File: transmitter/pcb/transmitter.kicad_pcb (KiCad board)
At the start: 2 copper layers, 70.5 x 67 mm, 14 parts, among them U1 AMS1117-3.3, U2 MOUDLE-SEEEDUINO-XIAO-ESP32C3

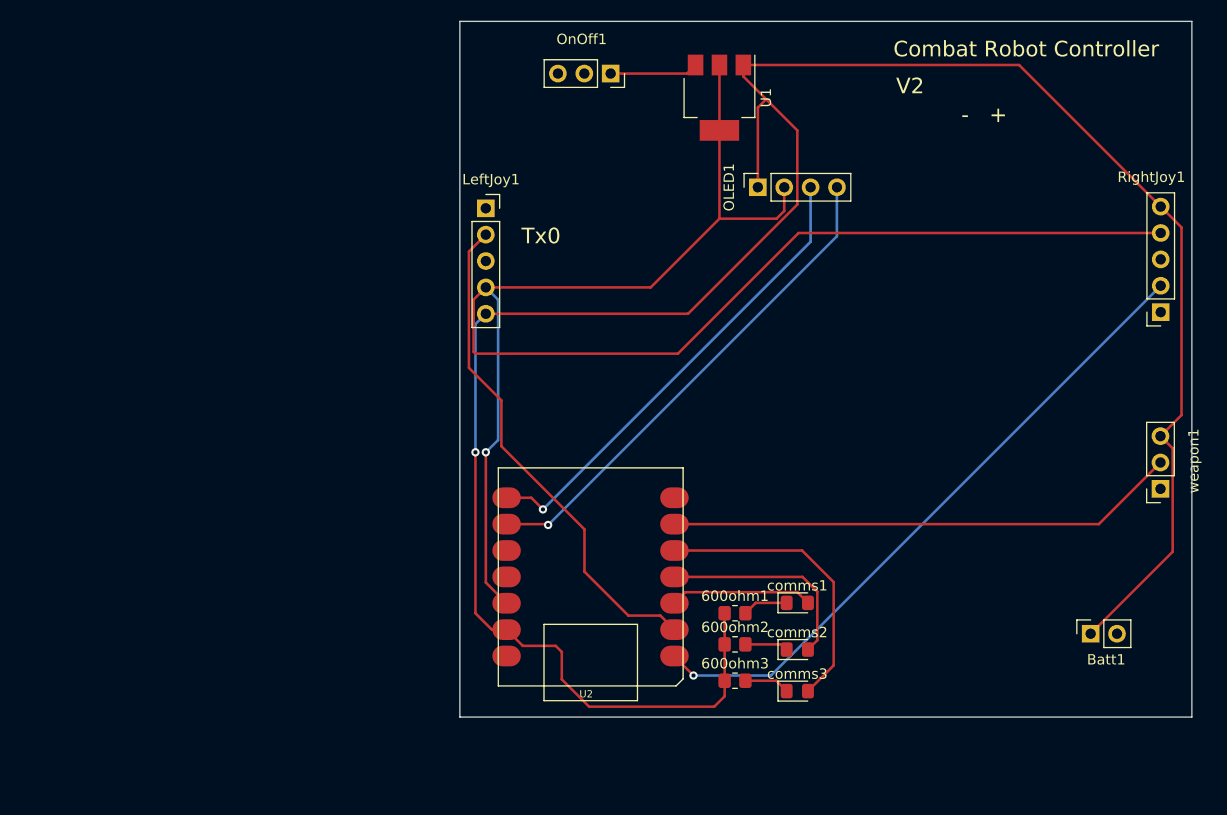
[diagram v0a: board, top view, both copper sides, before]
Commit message: Ready for Review
added trigger switches and joysticks

schematic is probably fine, but all of the route tracing needs to be redone

adjusted transmitter for ps4 geometry

added footprints

added passives adjusted pin assignment

ready for review
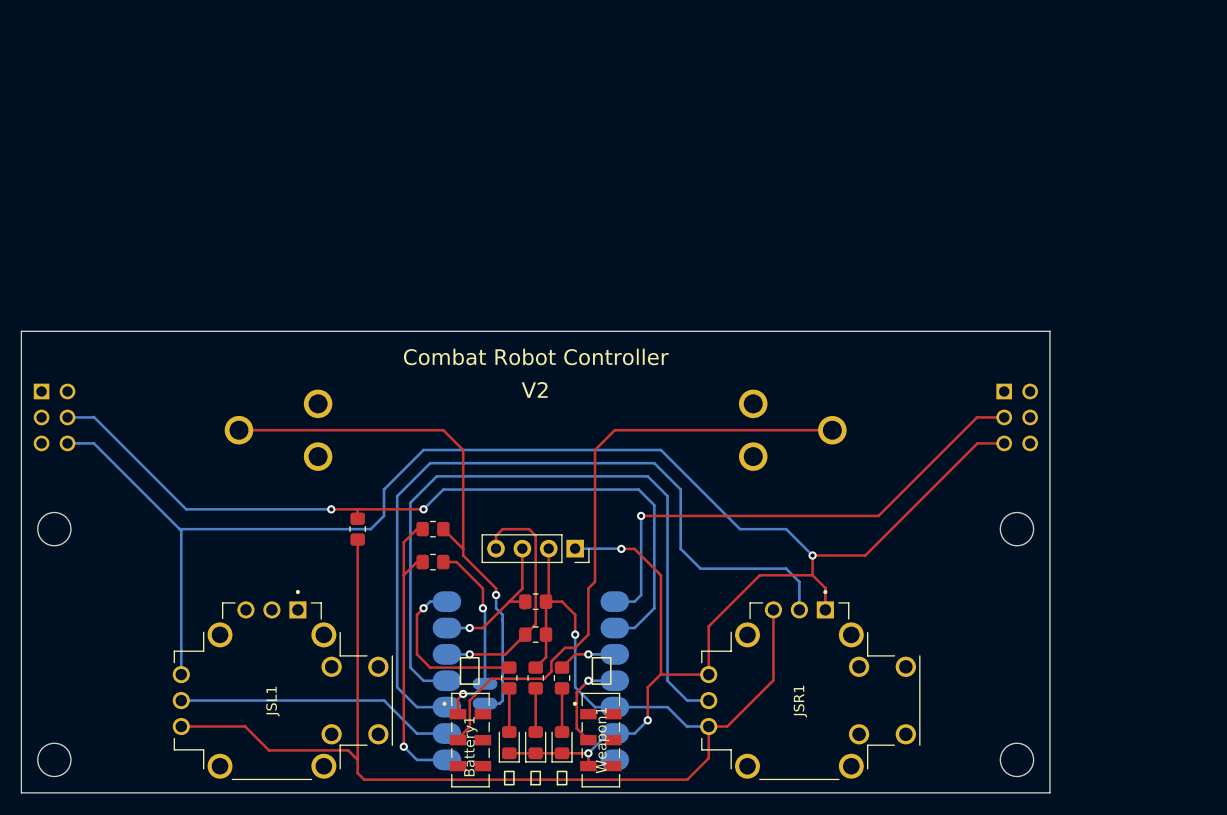
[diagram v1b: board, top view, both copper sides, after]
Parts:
- removed Batt1: j2, Connector_PinSocket_2.54mm:PinSocket_1x02_P2.54mm_Vertical
- removed LeftJoy1: J3, Connector_PinSocket_2.54mm:PinSocket_1x05_P2.54mm_Vertical
- removed RightJoy1: J4, Connector_PinSocket_2.54mm:PinSocket_1x05_P2.54mm_Vertical
- removed U1: AMS1117-3.3, Package_TO_SOT_SMD:SOT-223-3_TabPin2
- added 10kohm1: R_US, Resistor_SMD:R_0805_2012Metric_Pad1.20x1.40mm_HandSolder, F.Cu at (160.7, 88.9)
- added 2200ohm1: R_US, Resistor_SMD:R_0805_2012Metric_Pad1.20x1.40mm_HandSolder, F.Cu at (177.8, 95.9)
- added 2200ohm2: R_US, Resistor_SMD:R_0805_2012Metric_Pad1.20x1.40mm_HandSolder, F.Cu at (177.8, 99.1)
- added 220kohm1: R_US, Resistor_SMD:R_0805_2012Metric_Pad1.20x1.40mm_HandSolder, F.Cu at (167.9, 92.1)
- added 220kohm2: R_US, Resistor_SMD:R_0805_2012Metric_Pad1.20x1.40mm_HandSolder, F.Cu at (167.9, 88.9)
- added BT1: 54, SnapEDA Library:BAT_54, B.Cu at (202.6, 79.4)
- added BT2: 54, SnapEDA Library:BAT_54, B.Cu at (153.0, 79.4)
- added JSL1: THB001P, footprints:CNK_THB001P, F.Cu at (152.4, 105.4)
- added JSR1: THB001P, footprints:CNK_THB001P, F.Cu at (203.2, 105.4)
- added REF**: MountingHole_3.2mm_M3, MountingHole:MountingHole_3.2mm_M3, F.Cu at (131.4, 111.1)
- added REF**: MountingHole_3.2mm_M3, MountingHole:MountingHole_3.2mm_M3, F.Cu at (224.2, 88.9)
- added REF**: MountingHole_3.2mm_M3, MountingHole:MountingHole_3.2mm_M3, F.Cu at (224.2, 111.1)
- added REF**: MountingHole_3.2mm_M3, MountingHole:MountingHole_3.2mm_M3, F.Cu at (131.4, 88.9)
- added SL1: PBH2UEESNPNAGX, footprints:SW_PBH2UEESNPNAGX, B.Cu at (130.2, 75.6)
- added SR1: PBH2UEESNPNAGX, footprints:SW_PBH2UEESNPNAGX, B.Cu at (222.9, 75.6)
- Battery1: renamed from OnOff1; footprint Connector_PinSocket_2.54mm:PinSocket_1x03_P2.54mm_Vertical -> SnapEDA Library:SW_JS202011JCQN
- U2: moved to B.Cu
- Weapon1: renamed from weapon1; footprint Connector_PinSocket_2.54mm:PinSocket_1x03_P2.54mm_Vertical -> SnapEDA Library:SW_JS202011JCQN
- moved Battery1 65.6 mm to (171.5, 109.2), turned to 0 degrees
- moved Weapon1 59.1 mm to (184.1, 109.2), turned to 0 degrees
- moved OLED1 39.0 mm to (181.6, 90.8), turned to -90 degrees
- moved Fault1 30.8 mm to (175.3, 109.5), turned to 90 degrees
- moved Power1 25.7 mm to (177.8, 109.5), turned to 90 degrees
- moved U2 25.6 mm to (168.4, 93.0), turned to 0 degrees
- moved Comms1 24.4 mm to (180.3, 109.5), turned to 90 degrees
- moved 600ohm1 22.6 mm to (175.3, 103.2), turned to 90 degrees
- moved 600ohm3 19.2 mm to (177.8, 103.2), turned to 90 degrees
- moved 600ohm2 17.0 mm to (180.3, 103.2), turned to 90 degrees
- renumbered comms2 to Comms1, comms1 to Fault1, comms3 to Power1
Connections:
- 600ohm1 pad 1: GND -> Net-(Fault1-A)
- 600ohm1 pad 2: Net-(600ohm1-Pad2) -> Net-(U2-PB08_A6_D6_TX)
- 600ohm2 pad 1: GND -> Net-(Comms1-A)
- 600ohm2 pad 2: Net-(600ohm2-Pad2) -> Net-(U2-PA5_A9_D9_MISO)
- 600ohm3 pad 1: GND -> Net-(Power1-A)
- 600ohm3 pad 2: Net-(600ohm3-Pad2) -> +3.3V
- Battery1 pad 1: +9V -> Net-(U2-BAT+)
- Battery1 pad 2: +9V -> Net-(BT1-Pad1_3)
- Comms1 pad 1: Net-(600ohm2-Pad2) -> GND
- Comms1 pad 2: Net-(comms2-Pad2) -> Net-(Comms1-A)
- Fault1 pad 1: Net-(600ohm1-Pad2) -> GND
- Fault1 pad 2: Net-(comms1-Pad2) -> Net-(Fault1-A)
- OLED1 pad 3: Net-(OLED1-Pad3) -> Net-(OLED1-Pin_3)
- OLED1 pad 4: Net-(OLED1-Pad4) -> Net-(OLED1-Pin_4)
- Power1 pad 1: Net-(600ohm3-Pad2) -> GND
- Power1 pad 2: Net-(comms3-Pad2) -> Net-(Power1-A)
- U2 pad 10: unconnected-(U2-Pad10) -> Net-(U2-PA5_A9_D9_MISO)
- U2 pad 11: unconnected-(U2-Pad11) -> Net-(U2-PA6_A10_D10_MOSI)
- U2 pad 3: Net-(comms1-Pad2) -> Net-(U2-PA10_A2_D2)
- U2 pad 4: Net-(comms2-Pad2) -> Net-(U2-PA11_A3_D3)
- U2 pad 5: Net-(comms3-Pad2) -> Net-(OLED1-Pin_4)
- U2 pad 6: Net-(weapon1-Pad2) -> Net-(OLED1-Pin_3)
- U2 pad 7: unconnected-(U2-Pad7) -> Net-(U2-PB08_A6_D6_TX)
- U2 pad 8: Net-(OLED1-Pad3) -> Net-(U2-PB09_A7_D7_RX)
- U2 pad 9: Net-(OLED1-Pad4) -> Net-(U2-PA7_A8_D8_SCK)
- Weapon1 pad 2: Net-(weapon1-Pad2) -> Net-(U2-PA6_A10_D10_MOSI)
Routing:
- net Net-(U2-PA7_A8_D8_SCK): track 0.00 -> 77.0 mm, vias 0 -> 2
- net Net-(U2-PA10_A2_D2): track 0.00 -> 74.8 mm
- net Net-(U2-PA11_A3_D3): track 0.00 -> 69.1 mm
- net Net-(BT1-Pad1_3): track 0.00 -> 60.6 mm
- net Net-(U2-BAT-): track 0.00 -> 52.8 mm, vias 0 -> 1
- net Net-(U2-PB09_A7_D7_RX): track 0.00 -> 49.3 mm, vias 0 -> 1
- net Net-(weapon1-Pad2): track 49.3 -> 0.00 mm
- net Net-(OLED1-Pad4): track 48.1 -> 0.00 mm, vias 1 -> 0
- net Net-(OLED1-Pad3): track 45.7 -> 0.00 mm, vias 1 -> 0
- net Net-(U2-PA02_A0_D0): track 63.2 -> 29.0 mm
- net GND: track 218.1 -> 187.8 mm, vias 1 -> 4
- net Net-(comms3-Pad2): track 28.1 -> 0.00 mm
- net +3.3V: track 158.8 -> 130.8 mm
- net Net-(OLED1-Pin_4): track 0.00 -> 23.9 mm, vias 0 -> 1
- net Net-(U2-PA4_A1_D1): track 48.7 -> 27.4 mm
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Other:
- board size 70.5 x 67 mm -> 99.1 x 44.5 mm
- board text added: "+"
- board text added: "-"
- board text added: "18650 Battery Cell (3.7V)"
- board text added: ""
- board text added: ""
- board text added: ""
- board text added: ""
- board text added: ""
- board text removed: "- +"
- board text removed: "Tx0"

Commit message: V3 transmitter PCB
* moar resistor labels!
* re-routed analog inputs for joysticks, swapped a joystick sideways input for joystick click
* fixed improper use of a digital IO that needs to be an input
* battery connections are a through-pad...very excited to see if this works!
* spaced battery clips apart an extra 2.5mm
* added extra resistance to bring joystick voltages back into 2.5V range
* added some extra cutouts so we can use a 4 pole trigger button instead of 2 pole because its cheaper (momentary version)
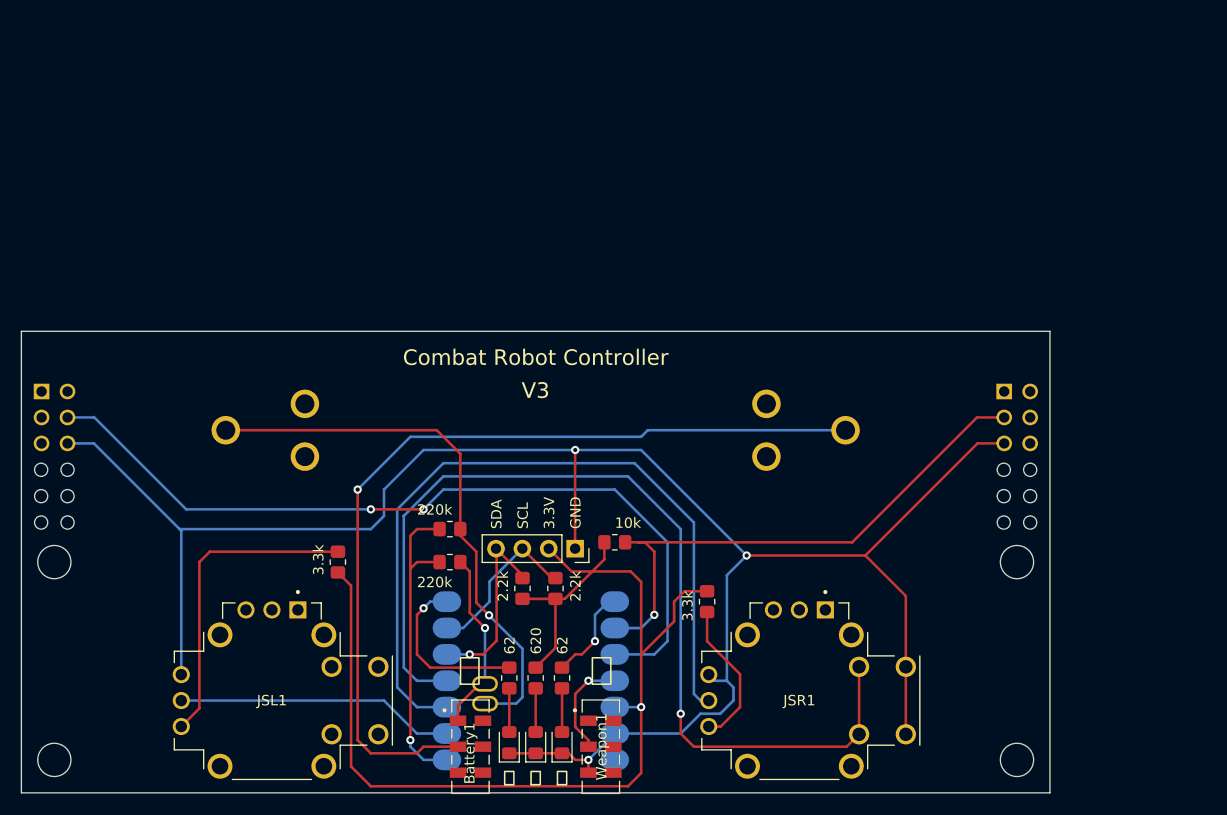
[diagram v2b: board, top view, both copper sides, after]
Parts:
- added 3300ohm1: R_US, Resistor_SMD:R_0805_2012Metric_Pad1.20x1.40mm_HandSolder, F.Cu at (158.8, 92.1)
- added 3300ohm2: R_US, Resistor_SMD:R_0805_2012Metric_Pad1.20x1.40mm_HandSolder, F.Cu at (194.3, 95.9)
- added ?: , , F.Cu at (132.7, 83.2)
- added ?: , , F.Cu at (222.9, 88.3)
- added ?: , , F.Cu at (222.9, 85.7)
- added ?: , , F.Cu at (132.7, 88.3)
- added ?: , , F.Cu at (225.4, 83.2)
- added ?: , , F.Cu at (222.9, 83.2)
- added ?: , , F.Cu at (130.2, 85.7)
- added ?: , , F.Cu at (225.4, 88.3)
- added ?: , , F.Cu at (130.2, 88.3)
- added ?: , , F.Cu at (132.7, 85.7)
- added ?: , , F.Cu at (130.2, 83.2)
- added ?: , , F.Cu at (225.4, 85.7)
- moved 10kohm1 24.8 mm to (185.4, 90.2), turned to 0 degrees
- moved 2200ohm2 4.62 mm to (176.5, 94.6), turned to -90 degrees
- moved REF** 3.17 mm to (224.2, 92.1)
- moved REF** 3.17 mm to (131.4, 92.1)
- moved 2200ohm1 2.29 mm to (179.7, 94.6), turned to -90 degrees
- moved 220kohm1 1.63 mm to (169.5, 92.1)
- moved 220kohm2 1.63 mm to (169.5, 88.9)
- moved BT1 1.27 mm to (203.8, 79.4)
- moved BT2 1.27 mm to (151.8, 79.4)
- moved Battery1 0.64 mm to (171.5, 109.9)
- moved Weapon1 0.64 mm to (184.1, 109.9)
- renumbered 600ohm3 to 620ohm3, 600ohm1 to 62ohm1, 600ohm2 to 62ohm2
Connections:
- 62ohm2 pad 2: Net-(U2-PA5_A9_D9_MISO) -> Net-(U2-PB09_A7_D7_RX)
- JSL1 pad VR2_3: +3.3V -> Net-(3300ohm1-Pad2)
- JSR1 pad A: (no net) -> Net-(U2-PA11_A3_D3)
- JSR1 pad B: (no net) -> Net-(U2-PA11_A3_D3)
- JSR1 pad C: (no net) -> GND
- JSR1 pad D: (no net) -> GND
- JSR1 pad VR1_1: GND -> (no net)
- JSR1 pad VR1_2: Net-(U2-PA10_A2_D2) -> (no net)
- JSR1 pad VR1_3: +3.3V -> (no net)
- JSR1 pad VR2_2: Net-(U2-PA11_A3_D3) -> Net-(U2-PA10_A2_D2)
- JSR1 pad VR2_3: +3.3V -> Net-(3300ohm2-Pad2)
- SL1 pad 5: Net-(U2-PA7_A8_D8_SCK) -> Net-(U2-PA5_A9_D9_MISO)
- SR1 pad 2: Net-(U2-PB09_A7_D7_RX) -> Net-(U2-PA7_A8_D8_SCK)
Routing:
- net Net-(U2-PA5_A9_D9_MISO): track 5.61 -> 79.5 mm, vias 1 -> 2
- net Net-(U2-PB09_A7_D7_RX): track 49.3 -> 9.20 mm
- net Net-(3300ohm1-Pad2): track 0.00 -> 30.3 mm
- net Net-(U2-PA11_A3_D3): track 69.1 -> 94.0 mm, vias 0 -> 1
- net Net-(BT1-Pad1_3): track 60.6 -> 83.9 mm, vias 0 -> 1
- net Net-(U2-PA7_A8_D8_SCK): track 77.0 -> 53.8 mm, vias 2 -> 1
- net +3.3V: track 130.8 -> 108.1 mm
- net Net-(3300ohm2-Pad2): track 0.00 -> 14.3 mm
- net Net-(OLED1-Pin_4): track 23.9 -> 18.1 mm
- net GND: track 187.8 -> 191.8 mm, vias 4 -> 3
- net Net-(OLED1-Pin_3): track 14.5 -> 15.9 mm, vias 1 -> 0
- net Net-(U2-BAT+): track 18.8 -> 17.6 mm, vias 2 -> 1
- net Net-(U2-PA10_A2_D2): track 74.8 -> 73.7 mm
- net Net-(U2-PA6_A10_D10_MOSI): track 9.19 -> 9.94 mm
- net unconnected-(SL1-Pad3): track 0.59 -> 0.00 mm
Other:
- board text added: "10k"
- board text added: "2.2k"
- board text added: "220k"
- board text added: "3.3V"
- board text added: "3.3k"
- board text added: "62"
- board text added: "620"
- board text added: "GND"
- board text added: "SCL"
- board text added: "SDA"
- board text added: "V3"
- board text removed: "V2"
